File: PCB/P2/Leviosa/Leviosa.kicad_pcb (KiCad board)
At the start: 2 copper layers, 80 x 80 mm, 52 parts, among them J1 2.54mm 1x03 Servo 1, J2 2.54mm 1x03 Servo 1, J3 2.54mm 1x03 Spare, J4 Barrel_Jack, Q3 TIP122, Q4 TIP122, U1 LM324, U2 ATtiny13A-P, U3 TPS1H200AQDGNRQ1, U5 L7805, U6 SS495A

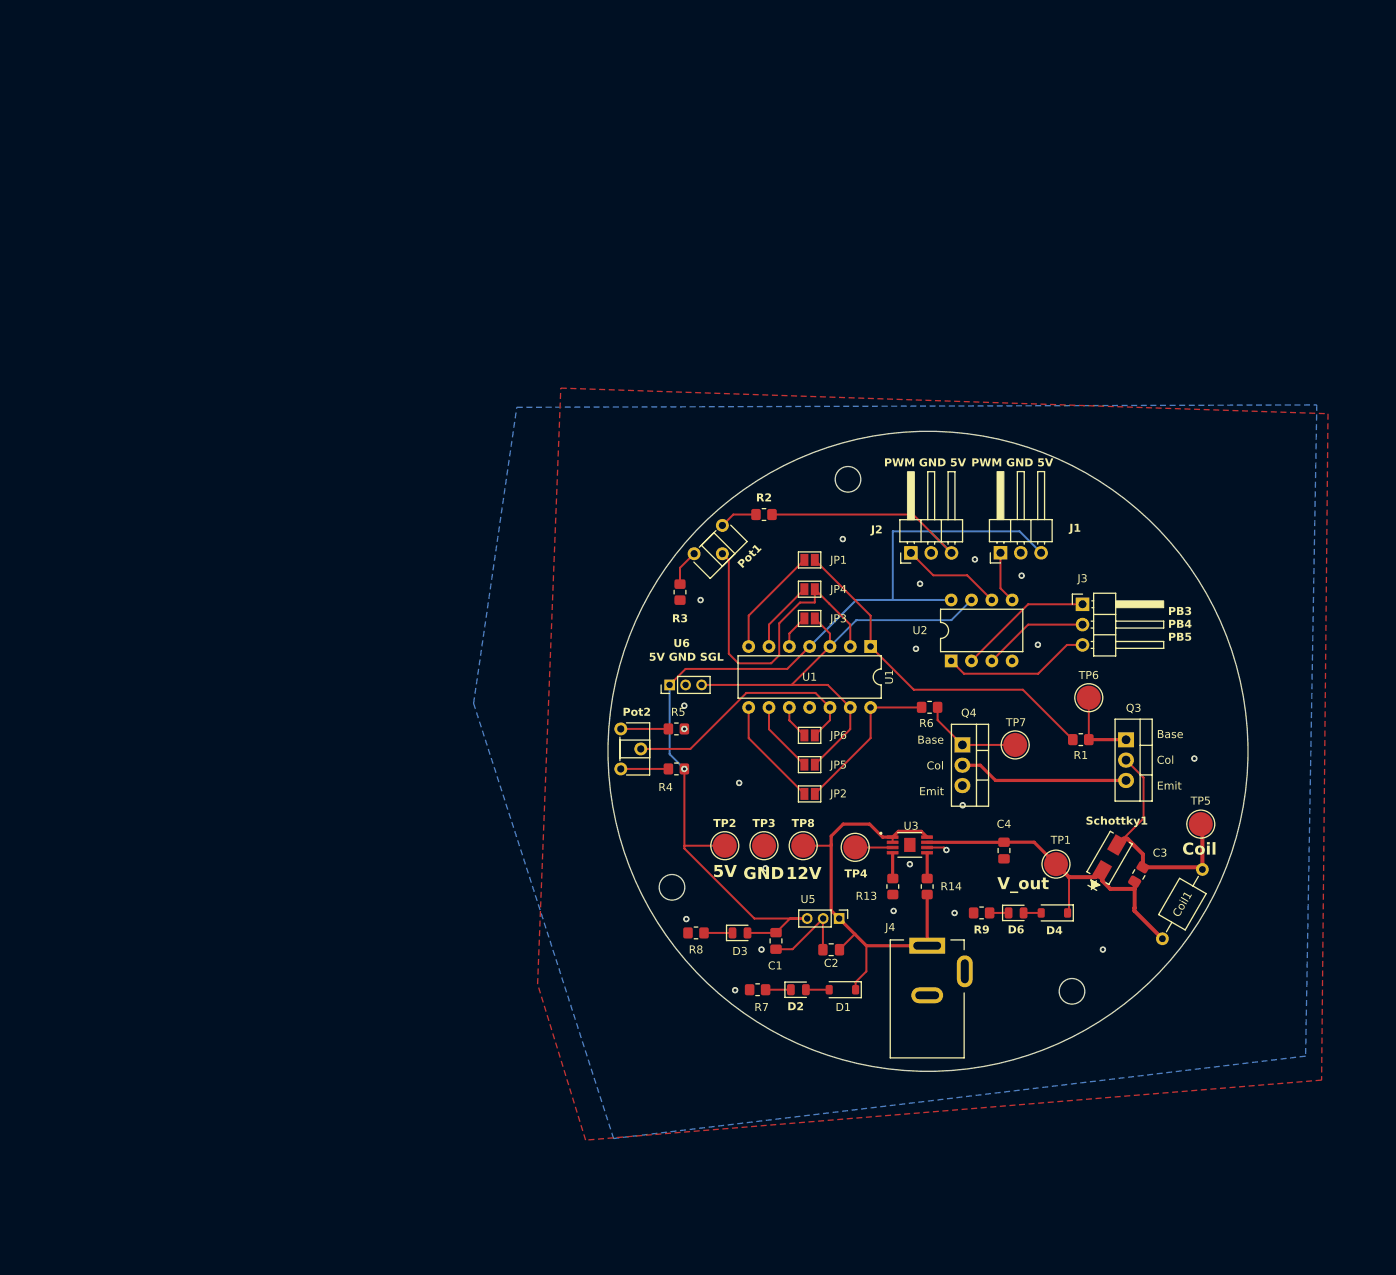
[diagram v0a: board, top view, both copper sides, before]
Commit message: update footprints, start pcb
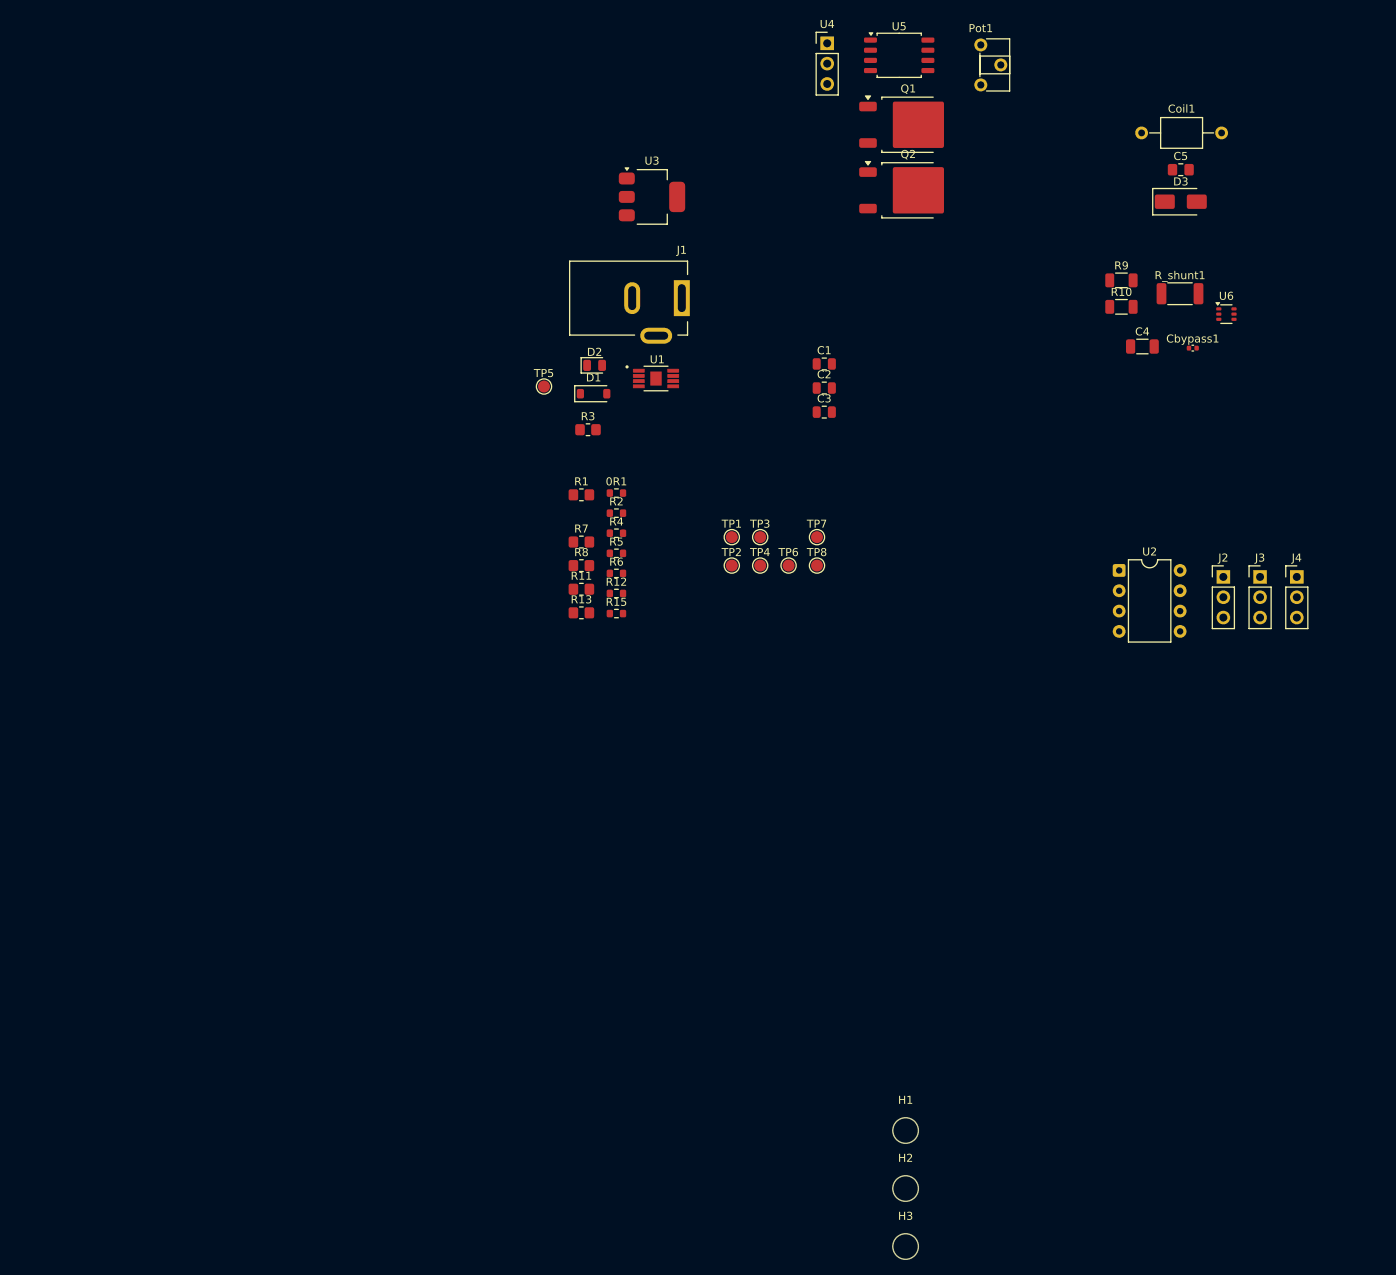
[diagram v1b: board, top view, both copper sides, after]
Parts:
- removed D4: BZT52C8V2 WD, Diode_SMD:D_SOD-123
- removed D6: LED, LED_SMD:LED_0805_2012Metric
- removed JP1, JP2, JP3, JP4, JP5, JP6: SolderJumper_2_Open, Jumper:SolderJumper-2_P1.3mm_Open_Pad1.0x1.5mm
- removed Pot2: 3362S-1-103LF, Potentiometer_THT:Potentiometer_ACP_CA6-H2,5_Horizontal
- removed Q3, Q4: TIP122, Package_TO_SOT_THT:TO-220-3_Vertical
- removed R14: 100kΩ, Resistor_SMD:R_0805_2012Metric_Pad1.20x1.40mm_HandSolder
- removed Schottky1: Schottky Diode SR206-TPCT-ND1, B230A_13_F:SMA_DIO
- added 0R1: DNP, Resistor_SMD:R_0603_1608Metric, F.Cu at (121.1, 87.7)
- added C5: 20nF, Capacitor_SMD:C_0805_2012Metric_Pad1.18x1.45mm_HandSolder, F.Cu at (191.6, 47.3)
- added Cbypass1: 0.1µF, Capacitor_SMD:C_0402_1005Metric, F.Cu at (193.1, 69.6)
- added Q1: NCE0110K, Package_TO_SOT_SMD:TO-252-2, F.Cu at (157.5, 41.7)
- added Q2: NCE0110K, Package_TO_SOT_SMD:TO-252-2, F.Cu at (157.5, 49.9)
- added R10: 8Ω, Resistor_SMD:R_1206_3216Metric, F.Cu at (184.2, 64.4)
- added R11: 54.2kΩ, Resistor_SMD:R_0805_2012Metric_Pad1.20x1.40mm_HandSolder, F.Cu at (116.7, 99.7)
- added R12: 3.9kΩ, Resistor_SMD:R_0603_1608Metric, F.Cu at (121.1, 100.3)
- added R15: 0Ω, Resistor_SMD:R_0603_1608Metric, F.Cu at (121.1, 102.8)
- added R_shunt1: 50mΩ, Resistor_SMD:R_2010_5025Metric, F.Cu at (191.5, 62.8)
- added U4: SS495A, Connector_PinHeader_2.54mm:PinHeader_1x03_P2.54mm_Vertical, F.Cu at (147.4, 31.5)
- C1: value 0.1µF -> 22µF; footprint Capacitor_SMD:C_0805_2012Metric_Pad1.18x1.45mm_HandSolder -> Capacitor_SMD:C_0805_2012Metric
- C2: value 0.33µF -> 22µF; footprint Capacitor_SMD:C_0805_2012Metric_Pad1.18x1.45mm_HandSolder -> Capacitor_SMD:C_0805_2012Metric
- C3: value 20nF -> 22µF; footprint Capacitor_SMD:C_0805_2012Metric_Pad1.18x1.45mm_HandSolder -> Capacitor_SMD:C_0805_2012Metric
- C4: value 10µF -> 47μF; footprint Capacitor_SMD:C_0805_2012Metric_Pad1.18x1.45mm_HandSolder -> Capacitor_SMD:C_1206_3216Metric
- D3: value LED -> SS34; footprint LED_SMD:LED_0805_2012Metric -> Diode_SMD:D_SMA
- J1: value 2.54mm 1x03 Servo 1 -> Barrel_Jack; footprint Connector_PinHeader_2.54mm:PinHeader_1x03_P2.54mm_Horizontal -> Connector_BarrelJack:BarrelJack_Kycon_KLDX-0202-xC_Horizontal
- J2: value 2.54mm 1x03 Servo 1 -> 2.54mm 1x03 Spare; footprint Connector_PinHeader_2.54mm:PinHeader_1x03_P2.54mm_Horizontal -> Connector_PinHeader_2.54mm:PinHeader_1x03_P2.54mm_Vertical
- J3: value 2.54mm 1x03 Spare -> 2.54mm 1x03 Servo 1; footprint Connector_PinHeader_2.54mm:PinHeader_1x03_P2.54mm_Horizontal -> Connector_PinHeader_2.54mm:PinHeader_1x03_P2.54mm_Vertical
- J4: value Barrel_Jack -> 2.54mm 1x03 Servo 1; footprint Connector_BarrelJack:BarrelJack_Kycon_KLDX-0202-xC_Horizontal -> Connector_PinHeader_2.54mm:PinHeader_1x03_P2.54mm_Vertical
- R1, R7: value 1kΩ -> 100kΩ
- R13: value 8kΩ -> 1kΩ
- R2: value 100kΩ -> 3.9kΩ; footprint Resistor_SMD:R_0805_2012Metric_Pad1.20x1.40mm_HandSolder -> Resistor_SMD:R_0603_1608Metric
- R3: value 7.8kΩ -> 1kΩ
- R4: value 100kΩ -> DNP; footprint Resistor_SMD:R_0805_2012Metric_Pad1.20x1.40mm_HandSolder -> Resistor_SMD:R_0603_1608Metric
- R5: value 54.2kΩ -> 0Ω; footprint Resistor_SMD:R_0805_2012Metric_Pad1.20x1.40mm_HandSolder -> Resistor_SMD:R_0603_1608Metric
- R6: value 1kΩ -> 51kΩ; footprint Resistor_SMD:R_0805_2012Metric_Pad1.20x1.40mm_HandSolder -> Resistor_SMD:R_0603_1608Metric
- R8: value 400 -> 1kΩ
- R9: value 1kΩ -> 8.2Ω; footprint Resistor_SMD:R_0805_2012Metric_Pad1.20x1.40mm_HandSolder -> Resistor_SMD:R_1206_3216Metric
- TP1: value Vout -> 12V; footprint TestPoint:TestPoint_Pad_D3.0mm -> TestPoint:TestPoint_Pad_D1.5mm
- TP2: value 5V -> GND; footprint TestPoint:TestPoint_Pad_D3.0mm -> TestPoint:TestPoint_Pad_D1.5mm
- TP3: value GND -> Fault; footprint TestPoint:TestPoint_Pad_D3.0mm -> TestPoint:TestPoint_Pad_D1.5mm
- TP4: value Fault -> 5V; footprint TestPoint:TestPoint_Pad_D3.0mm -> TestPoint:TestPoint_Pad_D1.5mm
- TP5: value coil_out -> Vout; footprint TestPoint:TestPoint_Pad_D3.0mm -> TestPoint:TestPoint_Pad_D1.5mm
- TP6, TP7: footprint TestPoint:TestPoint_Pad_D3.0mm -> TestPoint:TestPoint_Pad_D1.5mm
- TP8: value 12V -> coil_out; footprint TestPoint:TestPoint_Pad_D3.0mm -> TestPoint:TestPoint_Pad_D1.5mm
- U1: value LM324 -> TPS1H200AQDGNRQ1; footprint Package_DIP:DIP-14_W7.62mm -> TPS1H200AQDGNRQ1:SOP65P490X110-9N
- U3: value TPS1H200AQDGNRQ1 -> AMS1117-5.0; footprint TPS1H200AQDGNRQ1:SOP65P490X110-9N -> Package_TO_SOT_SMD:SOT-223-3_TabPin2
- U5: value L7805 -> LM393; footprint Connector_PinHeader_2.00mm:PinHeader_1x03_P2.00mm_Vertical -> Package_SO:SOIC-8_5.3x5.3mm_P1.27mm
- U6: value SS495A -> INA199xxDCK (50V/V); footprint Connector_PinHeader_2.00mm:PinHeader_1x03_P2.00mm_Vertical -> Package_TO_SOT_SMD:SOT-363_SC-70-6
- moved U5 108.2 mm to (156.4, 33.0), turned to 0 degrees
- moved D3 106.7 mm to (191.6, 51.3)
- moved Coil1 100.8 mm to (186.7, 42.7), turned to 0 degrees
- moved TP5 98.7 mm to (112.0, 74.4)
- moved U3 87.2 mm to (125.5, 50.7)
- moved U6 83.6 mm to (197.3, 65.3), turned to 0 degrees
- moved D2 82.1 mm to (118.3, 71.8)
- moved H1 81.7 mm to (157.2, 167.4)
- moved R9 81.0 mm to (184.2, 61.1), turned to 0 degrees
- moved D1 80.7 mm to (118.2, 75.3), turned to 0 degrees
- moved C1 72.4 mm to (147.0, 71.6), turned to 0 degrees
- moved C2 70.2 mm to (147.0, 74.6), turned to 0 degrees
- moved C3 69.9 mm to (147.0, 77.6), turned to 0 degrees
- moved R1 69.5 mm to (116.7, 87.9), turned to 0 degrees
- moved Pot1 68.2 mm to (166.6, 31.7), turned to 0 degrees
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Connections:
- C1 pad 1: /5V -> +12V
- C2 pad 1: +12V -> /V_out
- C3 pad 1: /V_out -> /5V
- C3 pad 2: /coil_output -> GND
- C4 pad 1: /V_out -> Net-(U6-+)
- C4 pad 2: GND -> Net-(U6--)
- Coil1 pad 1: /V_out -> Net-(D3-K)
- D1 pad 1: +12V -> /V_out
- D3 pad 2: /5V -> /coil_output
- J1 pad 1: /servo2_control -> +12V
- J1 pad 3: /5V -> (no net)
- J2 pad 1: /servo1_control -> /PB3
- J2 pad 2: GND -> /PB4
- J2 pad 3: /5V -> /PB5
- J3 pad 1: /PB3 -> /servo2_control
- J3 pad 2: /PB4 -> GND
- J3 pad 3: /PB5 -> /5V
- J4 pad 1: +12V -> /servo1_control
- J4 pad 3: (no net) -> /5V
- R1 pad 1: Net-(Q3-B) -> Net-(U1-DELAY)
- R1 pad 2: /set_point_trigger -> +12V
- R13 pad 1: GND -> Net-(Q2-G)
- R13 pad 2: Net-(U3-CL) -> /no_magnet_point_trigger
- R2 pad 1: Net-(Pot1-Pad1) -> GND
- R2 pad 2: /5V -> Net-(U1-CL)
- R3 pad 1: GND -> Net-(D2-K)
- R3 pad 2: Net-(Pot1-Pad3) -> GND
- R4 pad 1: Net-(Pot2-Pad3) -> Net-(U6-REF)
- R5 pad 2: Net-(Pot2-Pad1) -> Net-(U6-REF)
- R6 pad 1: Net-(Q4-B) -> Net-(Pot1-Pad3)
- R6 pad 2: /no_magnet_point_trigger -> /5V
- R7 pad 1: Net-(D2-K) -> /no_magnet_point
- R7 pad 2: GND -> /5V
- R8 pad 1: Net-(D3-K) -> Net-(Q1-G)
- R8 pad 2: GND -> /set_point_trigger
- R9 pad 1: Net-(D6-K) -> /V_out
- R9 pad 2: GND -> Net-(U6-+)
- TP1 pad 1: /V_out -> +12V
- TP2 pad 1: /5V -> GND
- TP3 pad 1: GND -> Net-(U1-~{FAULT})
- TP4 pad 1: Net-(U3-~{FAULT}) -> /5V
- TP5 pad 1: /coil_output -> /V_out
- TP6 pad 1: Net-(Q3-B) -> Net-(Q1-G)
- TP7 pad 1: Net-(Q4-B) -> Net-(Q2-G)
- TP8 pad 1: +12V -> /coil_output
- U1 pad 1: /set_point_trigger -> +12V
- U1 pad 2: /set_point -> +12V
- U1 pad 3: /PB2 -> Net-(U1-~{FAULT})
- U1 pad 4: /5V -> Net-(U1-CL)
- U1 pad 5: Net-(JP3-B) -> Net-(U1-DELAY)
- U1 pad 6: Net-(JP4-B) -> GND
- U1 pad 7: /spare_set_point_trigger -> /V_out
- U1 pad 8: /spare_no_magnet_point_trigger -> +12V
- U1 pad 9: Net-(JP5-A) -> GND
- U3 pad 1: +12V -> GND
- U3 pad 2: +12V -> /5V
- U3 pad 3: Net-(U3-~{FAULT}) -> +12V
- U5 pad 1: +12V -> /set_point_trigger
- U5 pad 2: GND -> /set_point
- U5 pad 3: /5V -> /hall_output
- U6 pad 1: /5V -> Net-(U6-REF)
- U6 pad 3: /PB2 -> /5V
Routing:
- net /5V: track 149.5 -> 0.00 mm, vias 1 -> 0
- net /PB2: track 59.9 -> 0.00 mm
- net +12V: track 56.4 -> 0.00 mm
- net /set_point_trigger: track 43.8 -> 0.00 mm
- net /V_out: track 43.0 -> 0.00 mm
- net /set_point: track 40.5 -> 0.00 mm
- net /coil_output: track 32.2 -> 0.00 mm
- net /no_magnet_point: track 31.6 -> 0.00 mm
- net /transistor1_output: track 21.2 -> 0.00 mm
- net /no_magnet_point_trigger: track 20.1 -> 0.00 mm
- net /PB5: track 18.6 -> 0.00 mm
- net /PB3: track 16.8 -> 0.00 mm
- net GND: track 14.0 -> 0.00 mm, vias 21 -> 0
- net /spare_set_point_trigger: track 13.7 -> 0.00 mm
- net /spare_no_magnet_point_trigger: track 13.7 -> 0.00 mm
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- removed copper zone on B.Cu, net GND
- removed copper zone on F.Cu, net GND
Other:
- board outline removed
- board text removed: "12V"
- board text removed: "5V"
- board text removed: "5V GND SGL"
- board text removed: "Base Col Emit"
- board text removed: "Coil"
- board text removed: "GND"
- board text removed: "PB3 PB4 PB5"
- board text removed: "PWM GND 5V"
- board text removed: "V_out"

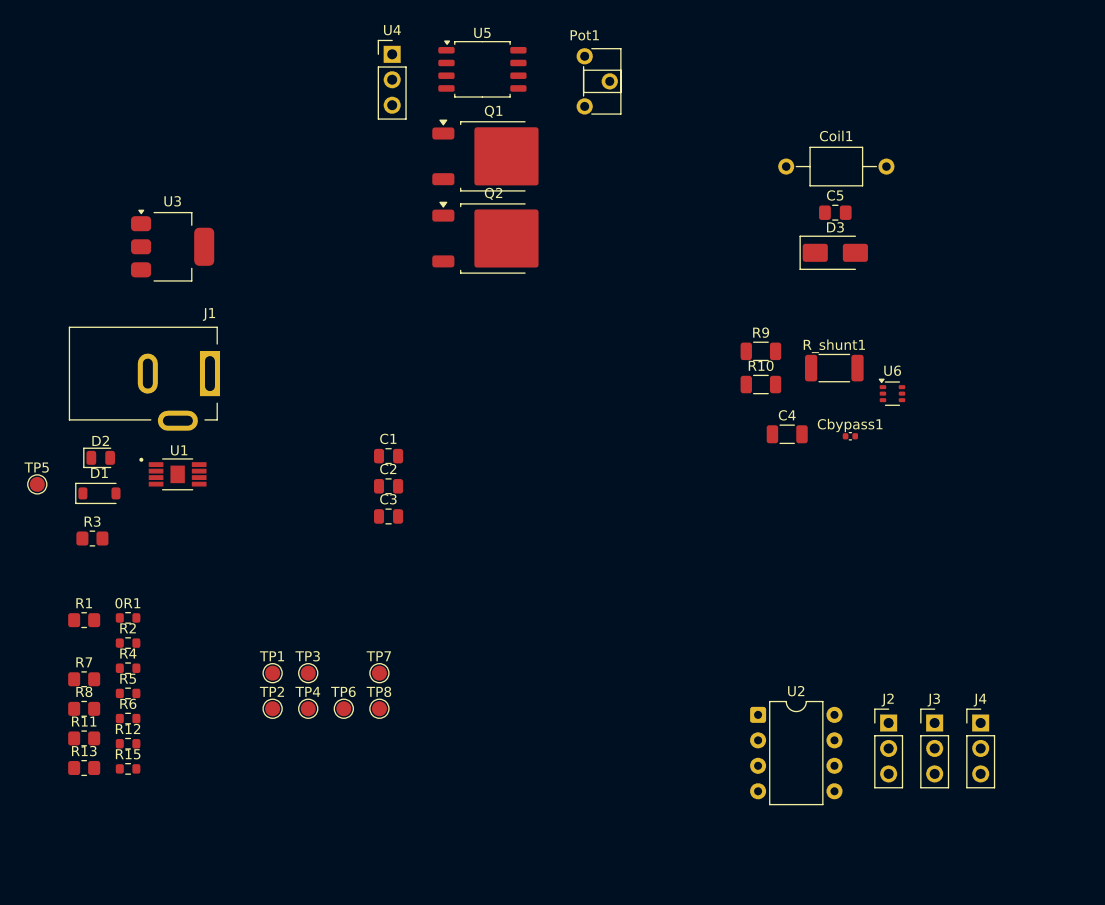
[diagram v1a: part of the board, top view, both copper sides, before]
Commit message: update node naming & PCB
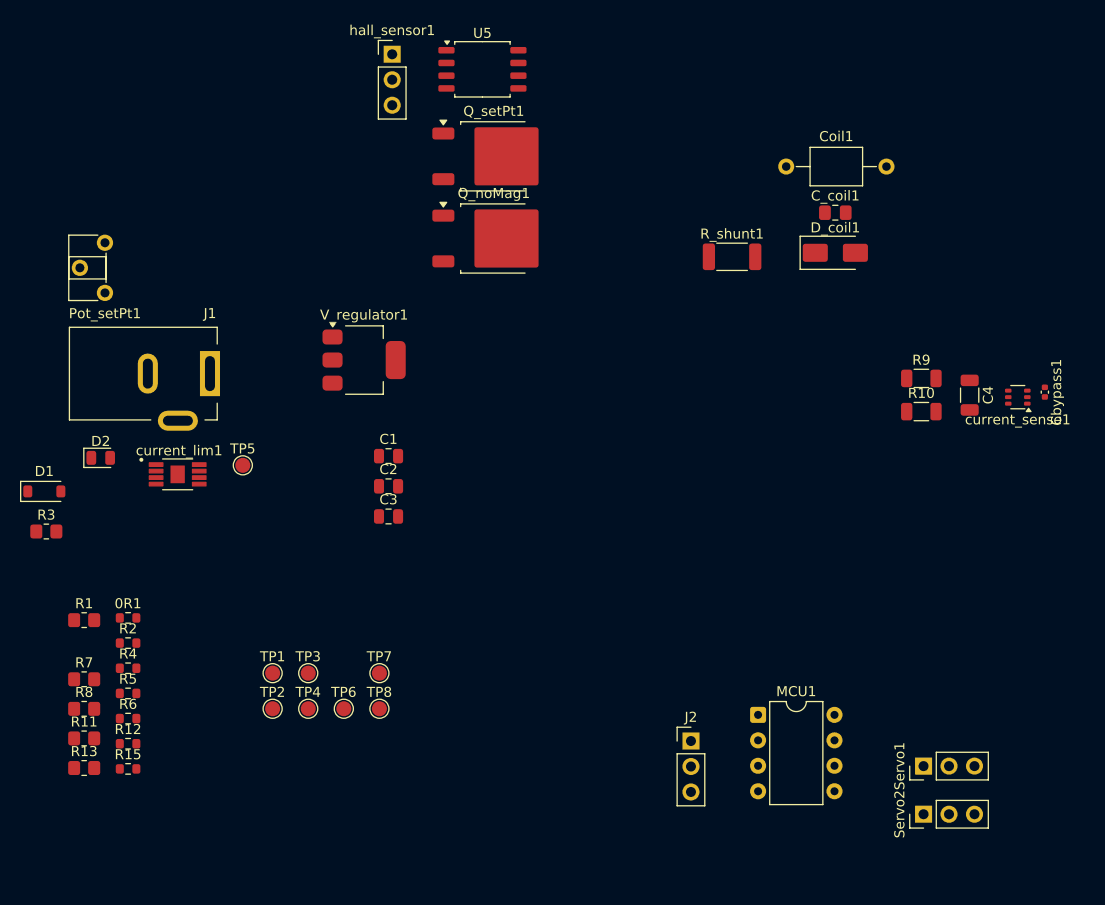
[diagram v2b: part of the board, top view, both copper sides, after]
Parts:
- moved Pot_setPt1 53.4 mm to (118.8, 55.3), turned to 180 degrees
- moved V_regulator1 22.2 mm to (144.6, 62.0)
- moved TP5 20.6 mm to (132.5, 72.5)
- moved Cbypass1 19.9 mm to (212.5, 65.2), turned to -90 degrees
- moved J2 19.8 mm to (177.2, 100.0)
- moved C4 18.6 mm to (205.0, 65.5), turned to -90 degrees
- moved R10 16.2 mm to (200.2, 67.1)
- moved R9 16.2 mm to (200.2, 63.8)
- moved R_shunt1 15.1 mm to (181.3, 51.7)
- moved current_sense1 12.5 mm to (209.8, 65.7), turned to 180 degrees
- moved Servo2 9.17 mm to (200.4, 107.3), turned to 90 degrees
- moved Servo1 7.14 mm to (200.4, 102.5), turned to 90 degrees
- moved D1 5.50 mm to (112.7, 75.1)
- moved R3 4.65 mm to (112.9, 79.1)
- renumbered C5 to C_coil1, D3 to D_coil1, U2 to MCU1, Pot1 to Pot_setPt1, Q2 to Q_noMag1, Q1 to Q_setPt1, J4 to Servo1, J3 to Servo2, U3 to V_regulator1, U1 to current_lim1, U6 to current_sense1, U4 to hall_sensor1
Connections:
- net /PB2 renamed /current_sense

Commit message: update PCB
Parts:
- moved Servo1 114.9 mm to (88.7, 129.5), turned to -90 degrees
- moved Servo2 113.1 mm to (88.7, 125.0), turned to -90 degrees
- moved Cbypass1 96.8 mm to (128.9, 114.0), turned to 180 degrees
- moved current_sense1 93.0 mm to (128.4, 110.7), turned to 90 degrees
- moved MCU1 90.2 mm to (101.7, 134.5), turned to 180 degrees
- moved C4 87.6 mm to (128.0, 107.3), turned to 0 degrees
- moved comparator 85.9 mm to (80.8, 73.7), turned to -90 degrees
- moved C2 83.1 mm to (75.2, 116.5), turned to -90 degrees
- moved R9 83.0 mm to (126.6, 102.3), turned to -90 degrees
- moved hall_sensor1 81.5 mm to (82.6, 80.9), turned to -90 degrees
- moved C_coil1 79.1 mm to (121.9, 84.8)
- moved R10 79.0 mm to (129.4, 102.3), turned to -90 degrees
- moved J2 77.9 mm to (106.3, 132.2), turned to 180 degrees
- moved D_coil1 77.8 mm to (123.4, 88.8)
- moved Coil1 76.4 mm to (120.9, 81.5), turned to 90 degrees
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- renumbered U5 to comparator
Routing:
- net /5V: track 0.00 -> 153.1 mm
- net /V_out: track 0.00 -> 76.5 mm
- net /coil_output: track 0.00 -> 56.6 mm
- net +12V: track 0.00 -> 55.5 mm
- net /current_sense: track 0.00 -> 53.1 mm
- net /set_point: track 0.00 -> 34.0 mm
- net Net-(Q_noMag1-G): track 0.00 -> 21.0 mm
- net Net-(D_coil1-K): track 0.00 -> 16.0 mm
- net /PB5: track 0.00 -> 14.2 mm
- net Net-(0R1-Pad1): track 0.00 -> 12.5 mm
- net /hall_output: track 0.00 -> 11.9 mm
- net Net-(Q_setPt1-G): track 0.00 -> 11.2 mm
- net /no_magnet_point: track 0.00 -> 9.74 mm
- net Net-(current_sense1-+): track 0.00 -> 9.69 mm
- net /no_magnet_point_trigger: track 0.00 -> 9.37 mm
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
